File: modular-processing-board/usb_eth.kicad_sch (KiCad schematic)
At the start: 18 parts, among them J401 TF01A, J801 TYPE-C-31-M-12, U401 SRV05-4

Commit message: checked components part numbers (next) board checks
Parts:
- C804, C805: LPN (none) -> C1530; MPN (none) -> 0402B221K500NT
- J801: LPN (none) -> C165948; MPN (none) -> TYPE-C-31-M-12
- R401, R402: LPN (none) -> C25804; MPN (none) -> 0603WAF1002T5E
- R804, R805: LPN (none) -> C23186; MPN (none) -> 0603WAF5101T5E
- R809, R810: LPN (none) -> C4216; MPN (none) -> 0603WAF3302T5E
- RN707: LPN (none) -> C29718; MPN (none) -> 4D03WGJ0103T5E
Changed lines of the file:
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@@
+			)
+		)
+		(property "LPN" "C4216"
+			(at 243.84 110.49 90)
+			(effects
+				(font
+					(size 1.27 1.27)
+				)
+				(hide yes)
+			)
+		)
+		(property "MPN" "0603WAF3302T5E"
+			(at 243.84 110.49 90)
+			(effects
+				(font
+					(size 1.27 1.27)
+				)
+				(hide yes)
 			)
 		)
@@
 		)
 		(property "Manufacturing Part Number" "0603WAF3302T5E"
+			(at 256.54 110.49 90)
+			(effects
+				(font
+					(size 1.27 1.27)
+				)
+				(hide yes)
+			)
+		)
+		(property "LPN" "C4216"
+			(at 256.54 110.49 90)
+			(effects
+				(font
+					(size 1.27 1.27)
+				)
+				(hide yes)
+			)
+		)
+		(property "MPN" "0603WAF3302T5E"
 			(at 256.54 110.49 90)
 			(effects
@@
 			)
 		)
+		(property "LPN" "C25804"
+			(at 119.38 86.36 90)
+			(effects
+				(font
+					(size 1.27 1.27)
+				)
+				(hide yes)
+			)
+		)
+		(property "MPN" "0603WAF1002T5E"
+			(at 119.38 86.36 90)
+			(effects
+				(font
+					(size 1.27 1.27)
+				)
+				(hide yes)
+			)
+		)
 		(pin "2"
 		)
@@
 			)
 		)
+		(property "LPN" "C25804"
+			(at 97.79 83.82 90)
+			(effects
+				(font
+					(size 1.27 1.27)
+				)
+				(hide yes)
+			)
+		)
+		(property "MPN" "0603WAF1002T5E"
+			(at 97.79 83.82 90)
+			(effects
+				(font
+					(size 1.27 1.27)
+				)
+				(hide yes)
+			)
+		)
 		(pin "2"
 		)
@@
 		)
 		(property "Manufacturing Part Number" "TYPE-C-31-M-12 "
+			(at 252.73 76.2 0)
+			(effects
+				(font
+					(size 1.27 1.27)
+				)
+				(hide yes)
+			)
+		)
+		(property "LPN" "C165948"
+			(at 252.73 76.2 0)
+			(effects
+				(font
+					(size 1.27 1.27)
+				)
+				(hide yes)
+			)
+		)
+		(property "MPN" "TYPE-C-31-M-12 "
 			(at 252.73 76.2 0)
 			(effects
@@
 			)
 		)
+		(property "LPN" "C1530"
+			(at 226.06 93.98 0)
+			(effects
+				(font
+					(size 1.27 1.27)
+				)
+				(hide yes)
+			)
+		)
+		(property "MPN" "0402B221K500NT"
+			(at 226.06 93.98 0)
+			(effects
+				(font
+					(size 1.27 1.27)
+				)
+				(hide yes)
+			)
+		)
 		(pin "2"
 		)
@@
 			)
 		)
+		(property "LPN" "C1530"
+			(at 213.36 93.98 0)
+			(effects
+				(font
+					(size 1.27 1.27)
+				)
+				(hide yes)
+			)
+		)
+		(property "MPN" "0402B221K500NT"
+			(at 213.36 93.98 0)
+			(effects
+				(font
+					(size 1.27 1.27)
+				)
+				(hide yes)
+			)
+		)
 		(pin "2"
 		)
@@
 		)
 		(property "Manufacturing Part Number" "0603WAF5101T5E"
+			(at 231.14 93.98 0)
+			(effects
+				(font
+					(size 1.27 1.27)
+				)
+				(hide yes)
+			)
+		)
+		(property "LPN" "C23186"
+			(at 231.14 93.98 0)
+			(effects
+				(font
+					(size 1.27 1.27)
+				)
+				(hide yes)
+			)
+		)
+		(property "MPN" "0603WAF5101T5E"
 			(at 231.14 93.98 0)
 			(effects
@@
 			)
 		)
+		(property "LPN" "C23186"
+			(at 219.71 93.98 0)
+			(effects
+				(font
+					(size 1.27 1.27)
+				)
+				(hide yes)
+			)
+		)
+		(property "MPN" "0603WAF5101T5E"
+			(at 219.71 93.98 0)
+			(effects
+				(font
+					(size 1.27 1.27)
+				)
+				(hide yes)
+			)
+		)
 		(pin "2"
 		)
@@
 			(at 107.95 80.01 0)
 			(effects
+				(font
+					(size 1.27 1.27)
+				)
+				(hide yes)
+			)
+		)
+		(property "LPN" "C29718"
+			(at 107.95 80.01 0)
+			(effects
+				(font
+					(size 1.27 1.27)
+				)
+				(hide yes)
+			)
+		)
+		(property "MPN" "4D03WGJ0103T5E"
+			(at 107.95 80.01 0)
+			(effects

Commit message: matched PSSI bus lenghts
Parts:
- C804, C805: LCSC Part Number C1530 -> (none); Manufacturing Part Number 0402B221K500NT -> (none)
- J801: LCSC Part Number C165948 -> (none); Manufacturing Part Number TYPE-C-31-M-12 -> (none)
- R401, R402: LCSC Part Number C25804 -> (none); Manufacturing Part Number 0603WAF1002T5E -> (none)
- R804, R805: LCSC Part Number C23186 -> (none); Manufacturing Part Number 0603WAF5101T5E -> (none)
- R809, R810: LCSC Part Number C4216 -> (none); Manufacturing Part Number 0603WAF3302T5E -> (none)
- RN707: LCSC Part Number C29718 -> (none); Manufacturing Part Number 4D03WGJ0103T5E -> (none)
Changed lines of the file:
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@@
-			)
-		)
-		(property "LCSC Part Number" "C4216"
-			(at 243.84 110.49 90)
-			(effects
-				(font
-					(size 1.27 1.27)
-				)
-				(hide yes)
-			)
-		)
-		(property "Manufacturing Part Number" "0603WAF3302T5E"
-			(at 243.84 110.49 90)
-			(effects
-				(font
-					(size 1.27 1.27)
-				)
-				(hide yes)
 			)
 		)
@@
 		)
 		(property "Availability" ""
-			(at 256.54 110.49 90)
-			(effects
-				(font
-					(size 1.27 1.27)
-				)
-				(hide yes)
-			)
-		)
-		(property "LCSC Part Number" "C4216"
-			(at 256.54 110.49 90)
-			(effects
-				(font
-					(size 1.27 1.27)
-				)
-				(hide yes)
-			)
-		)
-		(property "Manufacturing Part Number" "0603WAF3302T5E"
 			(at 256.54 110.49 90)
 			(effects
@@
 			)
 		)
-		(property "LCSC Part Number" "C25804"
-			(at 119.38 86.36 90)
-			(effects
-				(font
-					(size 1.27 1.27)
-				)
-				(hide yes)
-			)
-		)
-		(property "Manufacturing Part Number" "0603WAF1002T5E"
-			(at 119.38 86.36 90)
-			(effects
-				(font
-					(size 1.27 1.27)
-				)
-				(hide yes)
-			)
-		)
 		(property "LPN" "C25804"
 			(at 119.38 86.36 90)
@@
 			)
 		)
-		(property "LCSC Part Number" "C25804"
-			(at 97.79 83.82 90)
-			(effects
-				(font
-					(size 1.27 1.27)
-				)
-				(hide yes)
-			)
-		)
-		(property "Manufacturing Part Number" "0603WAF1002T5E"
-			(at 97.79 83.82 90)
-			(effects
-				(font
-					(size 1.27 1.27)
-				)
-				(hide yes)
-			)
-		)
 		(property "LPN" "C25804"
 			(at 97.79 83.82 90)
@@
 		)
 		(property "Availability" ""
-			(at 252.73 76.2 0)
-			(effects
-				(font
-					(size 1.27 1.27)
-				)
-				(hide yes)
-			)
-		)
-		(property "LCSC Part Number" "C165948"
-			(at 252.73 76.2 0)
-			(effects
-				(font
-					(size 1.27 1.27)
-				)
-				(hide yes)
-			)
-		)
-		(property "Manufacturing Part Number" "TYPE-C-31-M-12 "
 			(at 252.73 76.2 0)
 			(effects
@@
 			)
 		)
-		(property "LCSC Part Number" "C1530"
-			(at 226.06 93.98 0)
-			(effects
-				(font
-					(size 1.27 1.27)
-				)
-				(hide yes)
-			)
-		)
-		(property "Manufacturing Part Number" "0402B221K500NT"
-			(at 226.06 93.98 0)
-			(effects
-				(font
-					(size 1.27 1.27)
-				)
-				(hide yes)
-			)
-		)
 		(property "LPN" "C1530"
 			(at 226.06 93.98 0)
@@
 			)
 		)
-		(property "LCSC Part Number" "C1530"
-			(at 213.36 93.98 0)
-			(effects
-				(font
-					(size 1.27 1.27)
-				)
-				(hide yes)
-			)
-		)
-		(property "Manufacturing Part Number" "0402B221K500NT"
-			(at 213.36 93.98 0)
-			(effects
-				(font
-					(size 1.27 1.27)
-				)
-				(hide yes)
-			)
-		)
 		(property "LPN" "C1530"
 			(at 213.36 93.98 0)
@@
 		)
 		(property "Availability" ""
-			(at 231.14 93.98 0)
-			(effects
-				(font
-					(size 1.27 1.27)
-				)
-				(hide yes)
-			)
-		)
-		(property "LCSC Part Number" "C23186"
-			(at 231.14 93.98 0)
-			(effects
-				(font
-					(size 1.27 1.27)
-				)
-				(hide yes)
-			)
-		)
-		(property "Manufacturing Part Number" "0603WAF5101T5E"
 			(at 231.14 93.98 0)
 			(effects
@@
 			)
 		)
-		(property "LCSC Part Number" "C23186"
-			(at 219.71 93.98 0)
-			(effects
-				(font
-					(size 1.27 1.27)
-				)
-				(hide yes)
-			)
-		)
-		(property "Manufacturing Part Number" "0603WAF5101T5E"
-			(at 219.71 93.98 0)
-			(effects
-				(font
-					(size 1.27 1.27)
-				)
-				(hide yes)
-			)
-		)
 		(property "LPN" "C23186"
 			(at 219.71 93.98 0)
@@
 			(at 107.95 80.01 0)
 			(effects
-				(font
-					(size 1.27 1.27)
-				)
-				(hide yes)
-			)
-		)
-		(property "LCSC Part Number" "C29718"
-			(at 107.95 80.01 0)
-			(effects
-				(font
-					(size 1.27 1.27)
-				)
-				(hide yes)
-			)
-		)
-		(property "Manufacturing Part Number" "4D03WGJ0103T5E"
-			(at 107.95 80.01 0)
-			(effects

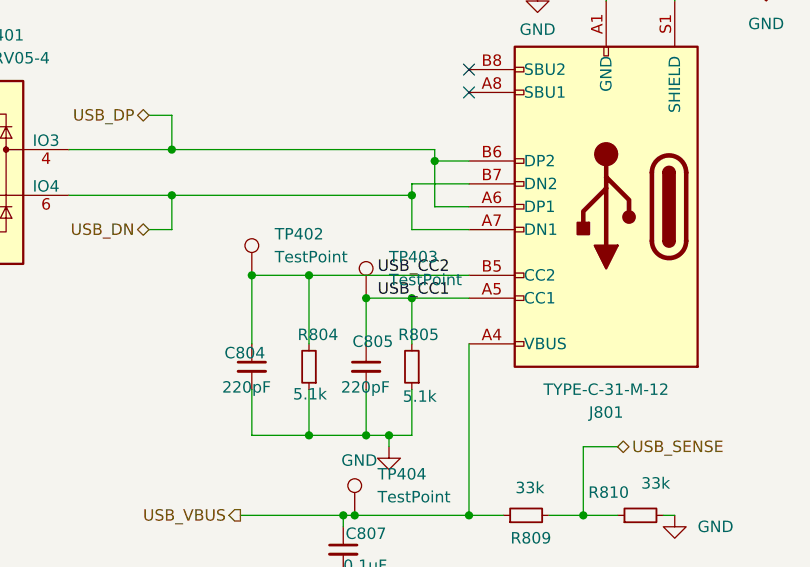
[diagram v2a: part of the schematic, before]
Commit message: finish modular-processing-hw board checks, prepare gerbers for manufacturing and perform checks
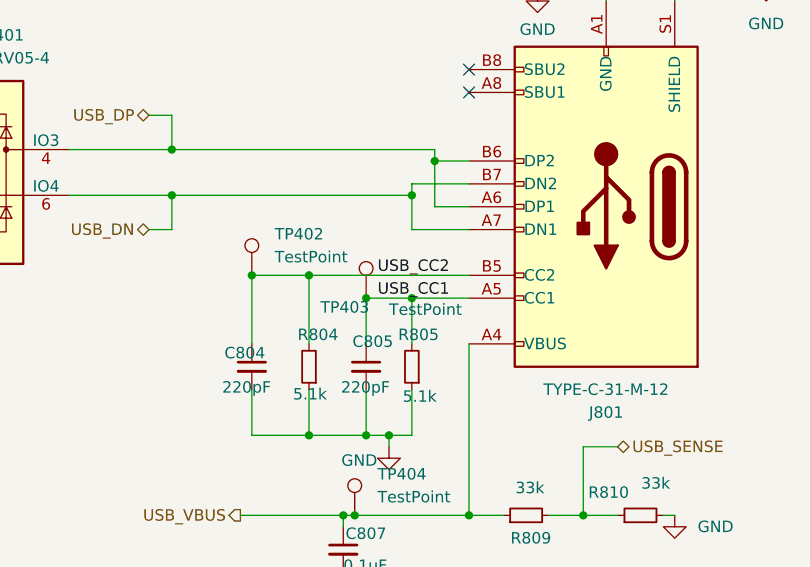
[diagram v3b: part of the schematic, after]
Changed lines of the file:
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@@
 		(on_board yes)
 		(dnp no)
-		(fields_autoplaced yes)
 		(property "Reference" "TP403"
-			(at 228.6 81.7879 0)
+			(at 220.98 87.3759 0)
 			(effects
 				(font
@@
 		)
 		(property "Value" "TestPoint"
-			(at 228.6 84.3279 0)
+			(at 228.6 87.6299 0)
 			(effects
 				(font

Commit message: minor changes in BOM and DNP-components
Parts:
- TP401, TP402, TP403, TP404: now left out of the parts list
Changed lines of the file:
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@@
 		(unit 1)
 		(exclude_from_sim no)
-		(in_bom yes)
+		(in_bom no)
 		(on_board yes)
 		(dnp no)
@@
 		(unit 1)
 		(exclude_from_sim no)
-		(in_bom yes)
+		(in_bom no)
 		(on_board yes)
 		(dnp no)
@@
 		(unit 1)
 		(exclude_from_sim no)
-		(in_bom yes)
+		(in_bom no)
 		(on_board yes)
 		(dnp no)
@@
 		(unit 1)
 		(exclude_from_sim no)
-		(in_bom yes)
-		(on_board yes)
-		(dnp no)
+		(in_bom no)
+		(on_board yes)
+		(dnp no)

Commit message: changed testpoints
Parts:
- TP401, TP402, TP403, TP404: footprint iw-misc:TestPoint_Pad_D0.5mm -> Connector_PinSocket_1.27mm:PinSocket_1x01_P1.27mm_Vertical
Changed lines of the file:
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@@
 			)
 		)
-		(property "Footprint" "iw-misc:TestPoint_Pad_D0.5mm"
+		(property "Footprint" "Connector_PinSocket_1.27mm:PinSocket_1x01_P1.27mm_Vertical"
 			(at 229.87 110.49 0)
 			(effects
@@
 			)
 		)
-		(property "Footprint" "iw-misc:TestPoint_Pad_D0.5mm"
+		(property "Footprint" "Connector_PinSocket_1.27mm:PinSocket_1x01_P1.27mm_Vertical"
 			(at 231.14 86.36 0)
 			(effects
@@
 			)
 		)
-		(property "Footprint" "iw-misc:TestPoint_Pad_D0.5mm"
+		(property "Footprint" "Connector_PinSocket_1.27mm:PinSocket_1x01_P1.27mm_Vertical"
 			(at 218.44 83.82 0)
 			(effects
@@
 			)
 		)
-		(property "Footprint" "iw-misc:TestPoint_Pad_D0.5mm"
+		(property "Footprint" "Connector_PinSocket_1.27mm:PinSocket_1x01_P1.27mm_Vertical"
 			(at 116.84 90.17 0)
 			(effects
